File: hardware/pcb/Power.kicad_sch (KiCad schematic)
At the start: 11 parts, among them J2 USB_B_Micro, U1 XC6808A4D28R-G, U3 NCP160AMX330TBG

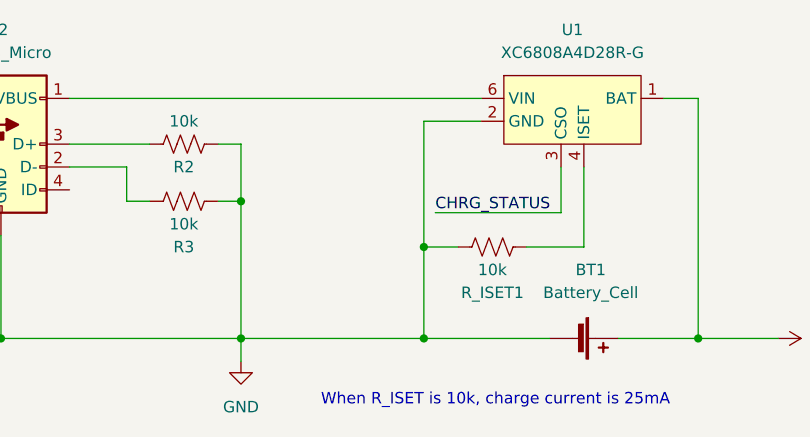
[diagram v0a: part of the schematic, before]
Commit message: Add amplifier to schematic
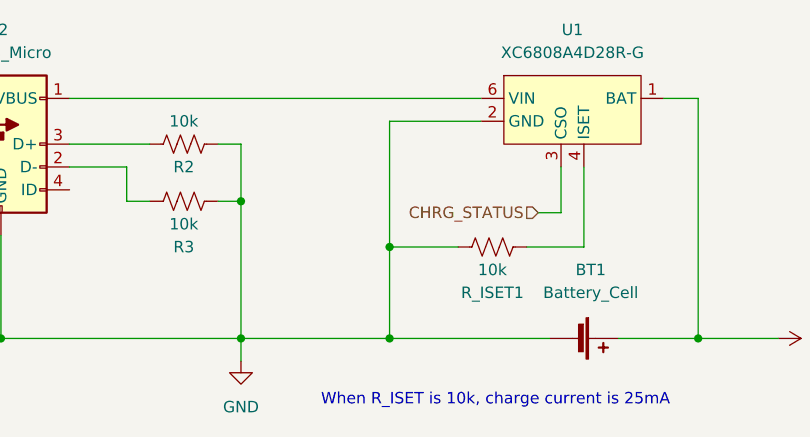
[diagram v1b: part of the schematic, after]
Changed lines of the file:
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@@
 (kicad_sch (version 20211123) (generator eeschema)
   (paper "A4")
+  (junction (at 100.33 109.22) (diameter 0) (color 0 0 0 0)
+  )
   (junction (at 134.62 109.22) (diameter 0) (color 0 0 0 0)
   )
   (junction (at 57.15 109.22) (diameter 0) (color 0 0 0 0)
   )
+  (junction (at 100.33 99.06) (diameter 0) (color 0 0 0 0)
+  )
   (junction (at 168.91 81.28) (diameter 0) (color 0 0 0 0)
-  )
-  (junction (at 104.14 109.22) (diameter 0) (color 0 0 0 0)
   )
   (junction (at 83.82 93.98) (diameter 0) (color 0 0 0 0)
@@
   (junction (at 191.77 96.52) (diameter 0) (color 0 0 0 0)
   )
-  (junction (at 104.14 99.06) (diameter 0) (color 0 0 0 0)
-  )
   (junction (at 204.47 81.28) (diameter 0) (color 0 0 0 0)
-  )
-  (wire (pts (xy 119.38 95.25) (xy 119.38 90.17))
-    (stroke (width 0) (type default) (color 0 0 0 0))
   )
   (wire (pts (xy 204.47 96.52) (xy 191.77 96.52))
@@
     (stroke (width 0) (type default) (color 0 0 0 0))
   )
-  (wire (pts (xy 104.14 99.06) (xy 104.14 109.22))
+  (wire (pts (xy 100.33 99.06) (xy 100.33 109.22))
     (stroke (width 0) (type default) (color 0 0 0 0))
   )
@@
     (stroke (width 0) (type default) (color 0 0 0 0))
   )
-  (wire (pts (xy 104.14 109.22) (xy 118.11 109.22))
-    (stroke (width 0) (type default) (color 0 0 0 0))
-  )
   (wire (pts (xy 191.77 99.06) (xy 191.77 96.52))
     (stroke (width 0) (type default) (color 0 0 0 0))
@@
     (stroke (width 0) (type default) (color 0 0 0 0))
   )
-  (wire (pts (xy 105.41 95.25) (xy 119.38 95.25))
+  (wire (pts (xy 204.47 92.71) (xy 204.47 96.52))
     (stroke (width 0) (type default) (color 0 0 0 0))
   )
-  (wire (pts (xy 204.47 92.71) (xy 204.47 96.52))
+  (wire (pts (xy 100.33 99.06) (xy 107.95 99.06))
     (stroke (width 0) (type default) (color 0 0 0 0))
   )
@@
     (stroke (width 0) (type default) (color 0 0 0 0))
   )
-  (wire (pts (xy 110.49 85.09) (xy 104.14 85.09))
+  (wire (pts (xy 110.49 85.09) (xy 100.33 85.09))
     (stroke (width 0) (type default) (color 0 0 0 0))
   )
@@
     (stroke (width 0) (type default) (color 0 0 0 0))
   )
+  (wire (pts (xy 100.33 109.22) (xy 118.11 109.22))
+    (stroke (width 0) (type default) (color 0 0 0 0))
+  )
   (wire (pts (xy 71.12 90.17) (xy 71.12 93.98))
     (stroke (width 0) (type default) (color 0 0 0 0))
@@
     (stroke (width 0) (type default) (color 0 0 0 0))
   )
+  (wire (pts (xy 119.38 90.17) (xy 119.38 95.25))
+    (stroke (width 0) (type default) (color 0 0 0 0))
+  )
   (wire (pts (xy 81.28 87.63) (xy 83.82 87.63))
+    (stroke (width 0) (type default) (color 0 0 0 0))
+  )
+  (wire (pts (xy 119.38 95.25) (xy 116.84 95.25))
     (stroke (width 0) (type default) (color 0 0 0 0))
   )
@@
     (stroke (width 0) (type default) (color 0 0 0 0))
   )
-  (wire (pts (xy 83.82 109.22) (xy 104.14 109.22))
+  (wire (pts (xy 83.82 109.22) (xy 100.33 109.22))
     (stroke (width 0) (type default) (color 0 0 0 0))
   )
@@
     (stroke (width 0) (type default) (color 0 0 0 0))
   )
-  (wire (pts (xy 104.14 99.06) (xy 107.95 99.06))
-    (stroke (width 0) (type default) (color 0 0 0 0))
-  )
-  (wire (pts (xy 104.14 85.09) (xy 104.14 99.06))
+  (wire (pts (xy 100.33 85.09) (xy 100.33 99.06))
     (stroke (width 0) (type default) (color 0 0 0 0))
   )
@@
     (effects (font (size 1.27 1.27)) (justify left bottom))
   )
-  (label "CHRG_STATUS" (at 105.41 95.25 0)
-    (effects (font (size 1.27 1.27)) (justify left bottom))
+  (hierarchical_label "CHRG_STATUS" (shape input) (at 116.84 95.25 180)
+    (effects (font (size 1.27 1.27)) (justify right))
   )
   (symbol (lib_id "power:GND") (at 191.77 111.76 0) (unit 1)

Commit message: Add schematic titles
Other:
- title: (none) -> Power
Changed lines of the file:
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@@
 (kicad_sch (version 20211123) (generator eeschema)
   (paper "A4")
+  (title_block
+    (title "Power")
+    (rev "1")
+  )
   (junction (at 100.33 109.22) (diameter 0) (color 0 0 0 0)
   )

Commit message: Assign some footprints. Not done.
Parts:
- BT1: footprint Package_DFN_QFN:OnSemi_XDFN4-1EP_1.0x1.0mm_EP0.52x0.52mm -> (none)
- C4: footprint (none) -> Capacitor_SMD:C_1206_3216Metric_Pad1.33x1.80mm_HandSolder
- MOSFET1: footprint SOT-23_TO-236_VIS -> Si2342DS:SI2342DS-T1-GE3
- R2, R3, R4: footprint (none) -> Resistor_SMD:R_1206_3216Metric_Pad1.30x1.75mm_HandSolder
- R_ISET1: footprint (none) -> Si2342DS:SI2342DS-T1-GE3
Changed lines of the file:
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@@
     (property "Reference" "BT1" (id 0) (at 122.682 101.6 90))
     (property "Value" "Battery_Cell" (id 1) (at 122.682 104.14 90))
-    (property "Footprint" "Package_DFN_QFN:OnSemi_XDFN4-1EP_1.0x1.0mm_EP0.52x0.52mm" (id 2) (at 122.174 109.22 90)
+    (property "Footprint" "" (id 2) (at 122.174 109.22 90)
       (effects (font (size 1.27 1.27)) hide)
     )
@@
     (property "Reference" "R2" (id 0) (at 77.47 90.17 90))
     (property "Value" "10k" (id 1) (at 77.47 85.09 90))
-    (property "Footprint" "" (id 2) (at 77.724 86.614 90)
+    (property "Footprint" "Resistor_SMD:R_1206_3216Metric_Pad1.30x1.75mm_HandSolder" (id 2) (at 77.724 86.614 90)
       (effects (font (size 1.27 1.27)) hide)
     )
@@
       (effects (font (size 1.27 1.27)) (justify left))
     )
-    (property "Footprint" "" (id 2) (at 169.926 87.884 90)
+    (property "Footprint" "Resistor_SMD:R_1206_3216Metric_Pad1.30x1.75mm_HandSolder" (id 2) (at 169.926 87.884 90)
       (effects (font (size 1.27 1.27)) hide)
     )
@@
     (property "Reference" "R_ISET1" (id 0) (at 111.76 104.14 90))
     (property "Value" "10k" (id 1) (at 111.76 101.6 90))
-    (property "Footprint" "" (id 2) (at 112.014 98.044 90)
+    (property "Footprint" "Si2342DS:SI2342DS-T1-GE3" (id 2) (at 112.014 98.044 90)
       (effects (font (size 1.27 1.27)) hide)
     )
@@
       (effects (font (size 1.524 1.524)) (justify left))
     )
-    (property "Footprint" "SOT-23_TO-236_VIS" (id 2) (at 195.58 110.744 0)
+    (property "Footprint" "Si2342DS:SI2342DS-T1-GE3" (id 2) (at 195.58 110.744 0)
       (effects (font (size 1.524 1.524)) hide)
     )
@@
       (effects (font (size 1.27 1.27)) (justify left))
     )
-    (property "Footprint" "" (id 2) (at 205.4352 92.71 0)
+    (property "Footprint" "Capacitor_SMD:C_1206_3216Metric_Pad1.33x1.80mm_HandSolder" (id 2) (at 205.4352 92.71 0)
       (effects (font (size 1.27 1.27)) hide)
     )
@@
     (property "Reference" "R3" (id 0) (at 77.47 99.06 90))
     (property "Value" "10k" (id 1) (at 77.47 96.52 90))
-    (property "Footprint" "" (id 2) (at 77.724 92.964 90)
+    (property "Footprint" "Resistor_SMD:R_1206_3216Metric_Pad1.30x1.75mm_HandSolder" (id 2) (at 77.724 92.964 90)
       (effects (font (size 1.27 1.27)) hide)
     )

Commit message: Finish footprint assignments (not final)
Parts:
- BT1: footprint (none) -> Connector_PinHeader_2.54mm:PinHeader_1x02_P2.54mm_Vertical
- D1: footprint (none) -> Package_TO_SOT_SMD:SOT-23
- J2: footprint (none) -> Connector_USB:USB_Micro-B_Amphenol_10118194_Horizontal
- R_ISET1: footprint Si2342DS:SI2342DS-T1-GE3 -> Resistor_SMD:R_1206_3216Metric_Pad1.30x1.75mm_HandSolder
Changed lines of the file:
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@@
     (property "Reference" "J2" (id 0) (at 57.15 74.93 0))
     (property "Value" "USB_B_Micro" (id 1) (at 57.15 77.47 0))
-    (property "Footprint" "" (id 2) (at 60.96 88.9 0)
+    (property "Footprint" "Connector_USB:USB_Micro-B_Amphenol_10118194_Horizontal" (id 2) (at 60.96 88.9 0)
       (effects (font (size 1.27 1.27)) hide)
     )
@@
     (property "Reference" "BT1" (id 0) (at 122.682 101.6 90))
     (property "Value" "Battery_Cell" (id 1) (at 122.682 104.14 90))
-    (property "Footprint" "" (id 2) (at 122.174 109.22 90)
+    (property "Footprint" "Connector_PinHeader_2.54mm:PinHeader_1x02_P2.54mm_Vertical" (id 2) (at 122.174 109.22 90)
       (effects (font (size 1.27 1.27)) hide)
     )
@@
       (effects (font (size 1.27 1.27)) (justify left))
     )
-    (property "Footprint" "" (id 2) (at 168.91 97.79 0)
+    (property "Footprint" "Package_TO_SOT_SMD:SOT-23" (id 2) (at 168.91 97.79 0)
       (effects (font (size 1.27 1.27)) hide)
     )
@@
     (property "Reference" "R_ISET1" (id 0) (at 111.76 104.14 90))
     (property "Value" "10k" (id 1) (at 111.76 101.6 90))
-    (property "Footprint" "Si2342DS:SI2342DS-T1-GE3" (id 2) (at 112.014 98.044 90)
+    (property "Footprint" "Resistor_SMD:R_1206_3216Metric_Pad1.30x1.75mm_HandSolder" (id 2) (at 112.014 98.044 90)
       (effects (font (size 1.27 1.27)) hide)
     )

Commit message: Add basic PCB outline
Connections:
- net -BATT renamed GND
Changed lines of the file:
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@@
   (junction (at 134.62 109.22) (diameter 0) (color 0 0 0 0)
   )
-  (junction (at 57.15 109.22) (diameter 0) (color 0 0 0 0)
-  )
   (junction (at 100.33 99.06) (diameter 0) (color 0 0 0 0)
   )
@@
   )
   (wire (pts (xy 191.77 109.22) (xy 191.77 111.76))
-    (stroke (width 0) (type default) (color 0 0 0 0))
-  )
-  (wire (pts (xy 50.8 109.22) (xy 57.15 109.22))
     (stroke (width 0) (type default) (color 0 0 0 0))
   )
@@
     (pin "3")
   )
-  (symbol (lib_id "power:-BATT") (at 50.8 109.22 90) (unit 1)
-    (in_bom yes) (on_board yes) (fields_autoplaced)
-    (property "Reference" "#PWR0101" (id 0) (at 54.61 109.22 0)
-      (effects (font (size 1.27 1.27)) hide)
-    )
-    (property "Value" "-BATT" (id 1) (at 46.99 109.2199 90)
-      (effects (font (size 1.27 1.27)) (justify left))
-    )
-    (property "Footprint" "" (id 2) (at 50.8 109.22 0)
-      (effects (font (size 1.27 1.27)) hide)
-    )
-    (property "Datasheet" "" (id 3) (at 50.8 109.22 0)
-      (effects (font (size 1.27 1.27)) hide)
-    )
-    (pin "1")
-  )
   (symbol (lib_id "Device:C") (at 204.47 88.9 0) (unit 1)

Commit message: Finish initial version of PCB
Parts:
- removed D1: 3V, Package_TO_SOT_SMD:SOT-23, symbol Device:D_Zener
- added D1: D_Zener_Dual_CommonAnode_KKA, Package_TO_SOT_SMD:SOT-23, symbol Device:D_Zener_Dual_CommonAnode_KKA
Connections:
- net at R4.2: now also D1.1 (K)
- net at MOSFET1.1: now also D1.3 (A)
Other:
- moved on the sheet: R4
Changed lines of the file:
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@@
   (junction (at 100.33 99.06) (diameter 0) (color 0 0 0 0)
   )
-  (junction (at 168.91 81.28) (diameter 0) (color 0 0 0 0)
+  (junction (at 158.75 81.28) (diameter 0) (color 0 0 0 0)
   )
   (junction (at 83.82 93.98) (diameter 0) (color 0 0 0 0)
@@
     (stroke (width 0) (type default) (color 0 0 0 0))
   )
-  (wire (pts (xy 168.91 81.28) (xy 168.91 83.82))
+  (wire (pts (xy 158.75 81.28) (xy 158.75 85.09))
     (stroke (width 0) (type default) (color 0 0 0 0))
   )
@@
     (stroke (width 0) (type default) (color 0 0 0 0))
   )
-  (wire (pts (xy 168.91 81.28) (xy 182.88 81.28))
-    (stroke (width 0) (type default) (color 0 0 0 0))
-  )
-  (wire (pts (xy 168.91 91.44) (xy 168.91 93.98))
+  (wire (pts (xy 158.75 81.28) (xy 182.88 81.28))
     (stroke (width 0) (type default) (color 0 0 0 0))
   )
@@
     (stroke (width 0) (type default) (color 0 0 0 0))
   )
+  (wire (pts (xy 158.75 92.71) (xy 158.75 96.52))
+    (stroke (width 0) (type default) (color 0 0 0 0))
+  )
   (wire (pts (xy 115.57 99.06) (xy 121.92 99.06))
     (stroke (width 0) (type default) (color 0 0 0 0))
@@
     (stroke (width 0) (type default) (color 0 0 0 0))
   )
-  (wire (pts (xy 160.02 81.28) (xy 168.91 81.28))
+  (wire (pts (xy 158.75 96.52) (xy 161.29 96.52))
+    (stroke (width 0) (type default) (color 0 0 0 0))
+  )
+  (wire (pts (xy 147.32 81.28) (xy 158.75 81.28))
     (stroke (width 0) (type default) (color 0 0 0 0))
   )
@@
     (pin "4")
     (pin "5")
-  )
-  (symbol (lib_id "Device:D_Zener") (at 168.91 97.79 270) (unit 1)
-    (in_bom yes) (on_board yes) (fields_autoplaced)
-    (property "Reference" "D1" (id 0) (at 171.45 96.5199 90)
-      (effects (font (size 1.27 1.27)) (justify left))
-    )
-    (property "Value" "3V" (id 1) (at 171.45 99.0599 90)
-      (effects (font (size 1.27 1.27)) (justify left))
-    )
-    (property "Footprint" "Package_TO_SOT_SMD:SOT-23" (id 2) (at 168.91 97.79 0)
-      (effects (font (size 1.27 1.27)) hide)
-    )
-    (property "Datasheet" "~" (id 3) (at 168.91 97.79 0)
-      (effects (font (size 1.27 1.27)) hide)
-    )
-    (pin "1")
-    (pin "2")
   )
   (symbol (lib_id "Device:R_US") (at 77.47 87.63 90) (unit 1)
@@
     (pin "2")
   )
-  (symbol (lib_id "power:+BATT") (at 160.02 81.28 90) (unit 1)
-    (in_bom yes) (on_board yes) (fields_autoplaced)
-    (property "Reference" "#PWR0110" (id 0) (at 163.83 81.28 0)
-      (effects (font (size 1.27 1.27)) hide)
-    )
-    (property "Value" "+BATT" (id 1) (at 156.21 81.2799 90)
-      (effects (font (size 1.27 1.27)) (justify left))
-    )
-    (property "Footprint" "" (id 2) (at 160.02 81.28 0)
-      (effects (font (size 1.27 1.27)) hide)
-    )
-    (property "Datasheet" "" (id 3) (at 160.02 81.28 0)
-      (effects (font (size 1.27 1.27)) hide)
-    )
-    (pin "1")
-  )
-  (symbol (lib_id "Device:R_US") (at 168.91 87.63 0) (unit 1)
-    (in_bom yes) (on_board yes) (fields_autoplaced)
-    (property "Reference" "R4" (id 0) (at 171.45 86.3599 0)
-      (effects (font (size 1.27 1.27)) (justify left))
-    )
-    (property "Value" "10" (id 1) (at 171.45 88.8999 0)
-      (effects (font (size 1.27 1.27)) (justify left))
-    )
-    (property "Footprint" "Resistor_SMD:R_1206_3216Metric_Pad1.30x1.75mm_HandSolder" (id 2) (at 169.926 87.884 90)
-      (effects (font (size 1.27 1.27)) hide)
-    )
-    (property "Datasheet" "~" (id 3) (at 168.91 87.63 0)
+  (symbol (lib_id "power:+BATT") (at 147.32 81.28 90) (unit 1)
+    (in_bom yes) (on_board yes) (fields_autoplaced)
+    (property "Reference" "#PWR0110" (id 0) (at 151.13 81.28 0)
+      (effects (font (size 1.27 1.27)) hide)
+    )
+    (property "Value" "+BATT" (id 1) (at 143.51 81.2799 90)
+      (effects (font (size 1.27 1.27)) (justify left))
+    )
+    (property "Footprint" "" (id 2) (at 147.32 81.28 0)
+      (effects (font (size 1.27 1.27)) hide)
+    )
+    (property "Datasheet" "" (id 3) (at 147.32 81.28 0)
+      (effects (font (size 1.27 1.27)) hide)
+    )
+    (pin "1")
+  )
+  (symbol (lib_id "Device:R_US") (at 158.75 88.9 0) (unit 1)
+    (in_bom yes) (on_board yes) (fields_autoplaced)
+    (property "Reference" "R4" (id 0) (at 161.29 87.6299 0)
+      (effects (font (size 1.27 1.27)) (justify left))
+    )
+    (property "Value" "10" (id 1) (at 161.29 90.1699 0)
+      (effects (font (size 1.27 1.27)) (justify left))
+    )
+    (property "Footprint" "Resistor_SMD:R_1206_3216Metric_Pad1.30x1.75mm_HandSolder" (id 2) (at 159.766 89.154 90)
+      (effects (font (size 1.27 1.27)) hide)
+    )
+    (property "Datasheet" "~" (id 3) (at 158.75 88.9 0)
       (effects (font (size 1.27 1.27)) hide)
     )
@@
     (pin "2")
   )
+  (symbol (lib_id "Device:D_Zener_Dual_CommonAnode_KKA") (at 168.91 96.52 0) (unit 1)
+    (in_bom yes) (on_board yes) (fields_autoplaced)
+    (property "Reference" "D1" (id 0) (at 168.91 90.17 0))
+    (property "Value" "D_Zener_Dual_CommonAnode_KKA" (id 1) (at 168.91 92.71 0))
+    (property "Footprint" "Package_TO_SOT_SMD:SOT-23" (id 2) (at 168.91 96.52 0)
+      (effects (font (size 1.27 1.27)) hide)
+    )
+    (property "Datasheet" "~" (id 3) (at 168.91 96.52 0)
+      (effects (font (size 1.27 1.27)) hide)
+    )
+    (pin "1")
+    (pin "2")
+    (pin "3")
+  )
   (symbol (lib_id "Device:R_US") (at 77.47 93.98 90) (unit 1)

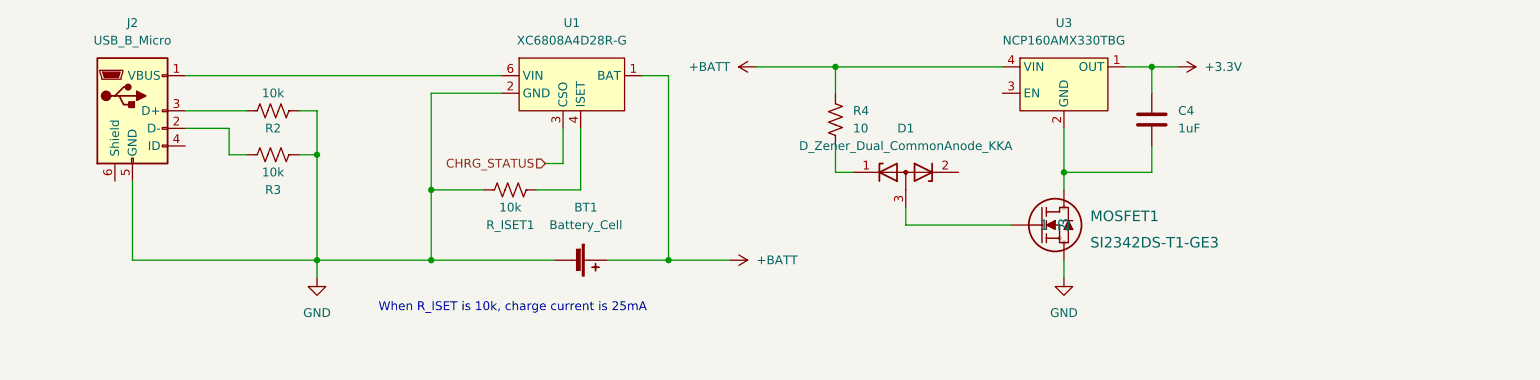
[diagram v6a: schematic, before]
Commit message: Add power switch and redo overdischarge circuit
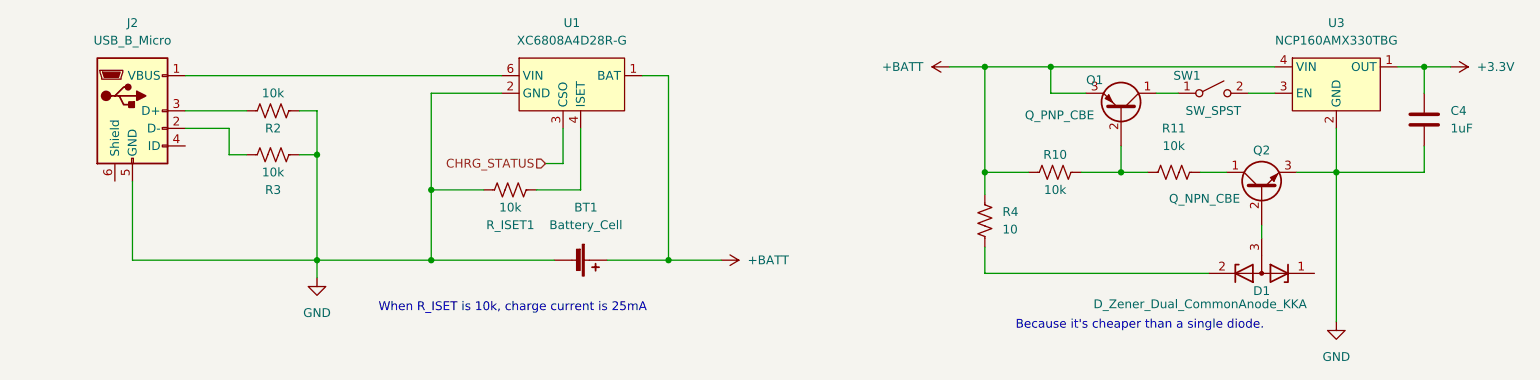
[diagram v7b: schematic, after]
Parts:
- removed MOSFET1: SI2342DS-T1-GE3, Si2342DS:SI2342DS-T1-GE3, symbol Si2342DS:SI2342DS-T1-GE3
- added Q1: Q_PNP_CBE, symbol Device:Q_PNP_CBE
- added Q2: Q_NPN_CBE, symbol Device:Q_NPN_CBE
- added R10, R11: 10k, symbol Device:R_US
- added SW1: SW_SPST, symbol Switch:SW_SPST
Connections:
- net +BATT: now also Q1.3 (E), R10.1
- net GND: now also C4.2, U3.2 (GND), U3.5 (EPAD), Q2.3 (E)
- net at U3.3 (EN): now also SW1.2 (B)
- net at R4.2: now also D1.2 (K); no longer D1.1 (K)
- net at D1.3 (A): now also Q2.2 (B)
- new net: Q1.2 (B), R10.2, R11.1
- new net: Q2.1 (C), R11.2
- new net: Q1.1 (C), SW1.1 (A)
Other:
- note added: "Because it's cheaper than a single diode."
- moved on the sheet: C4, D1, R4, U3
